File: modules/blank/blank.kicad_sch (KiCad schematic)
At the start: 8 parts

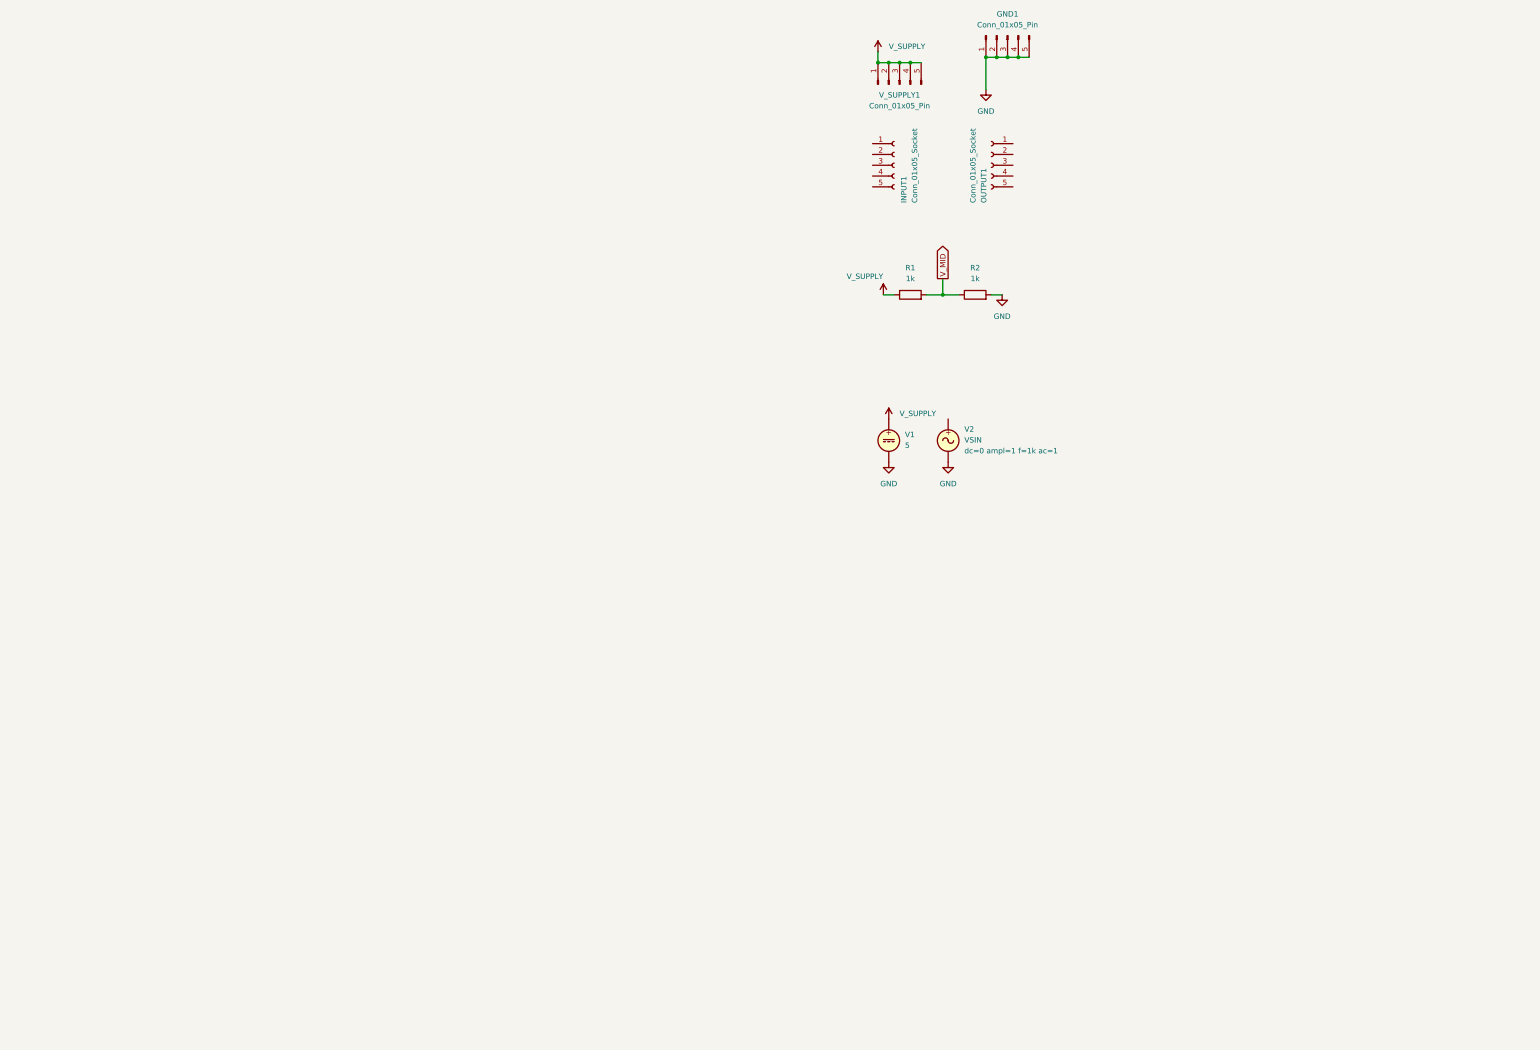
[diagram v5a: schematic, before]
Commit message: blank:Add opamp & pot as a built-in components These are used in almost all the projects. So, having pre-build components make is easy to get started
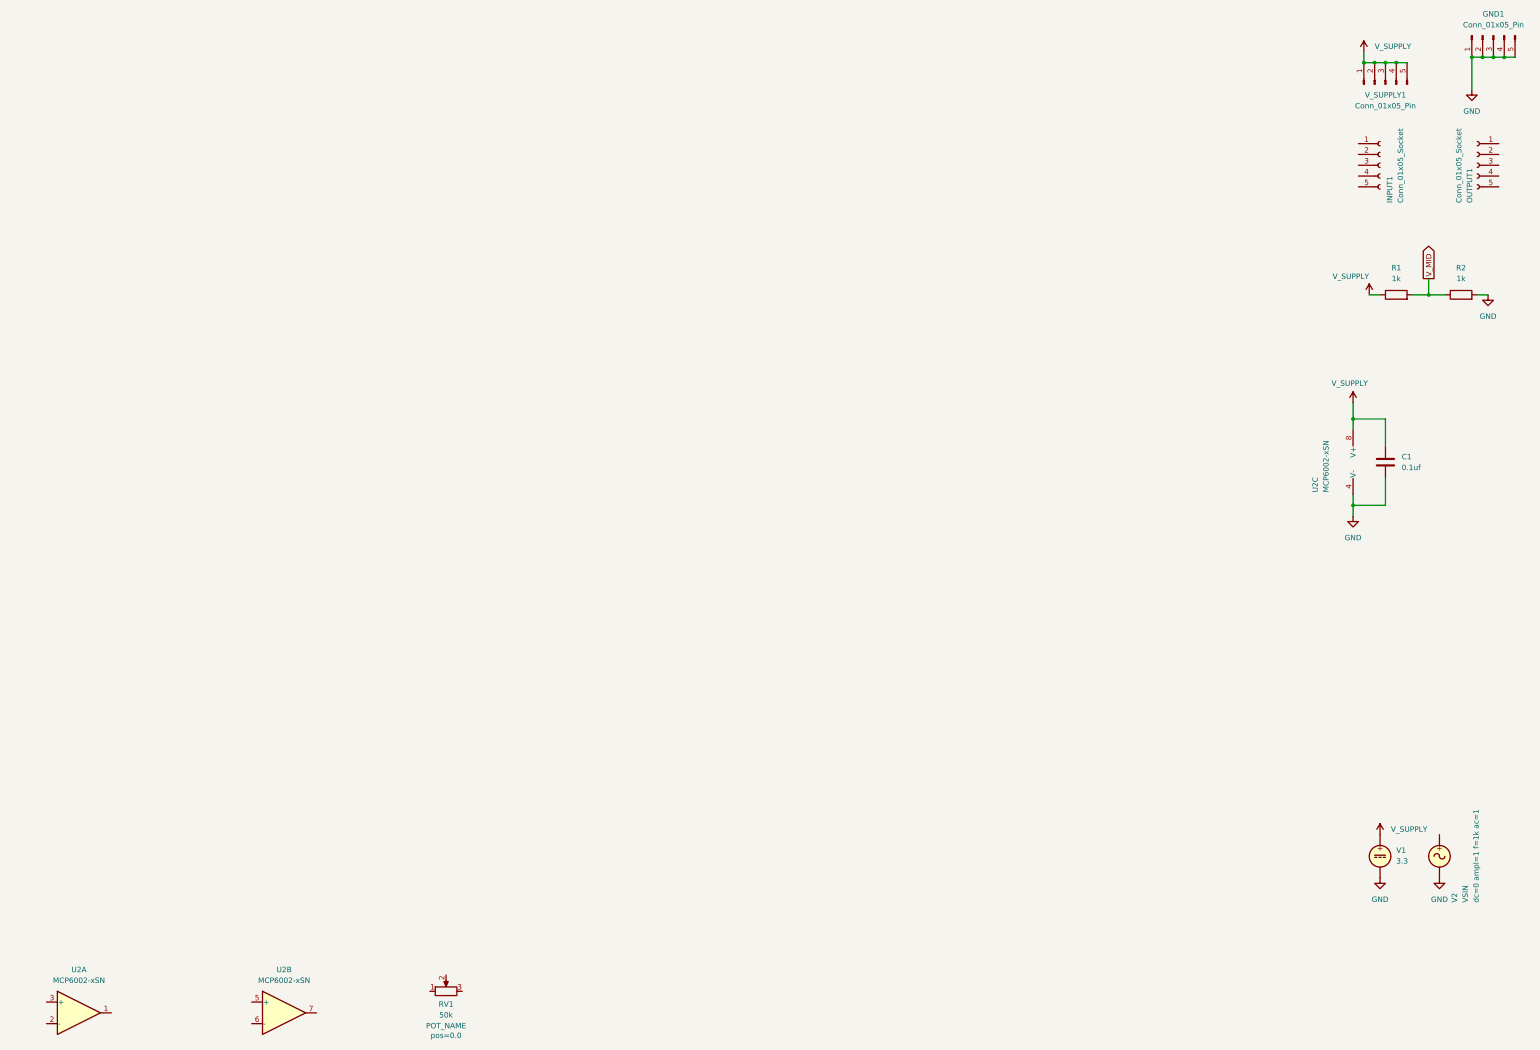
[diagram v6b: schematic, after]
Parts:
- added C1: 0.1uf, symbol Device:C
- added RV1: 50k, BreadModular_Pots:Potentiometer_RV09, symbol Device:R_Potentiometer
- added U2: MCP6002-xSN, Package_SO:SOIC-8-1EP_3.9x4.9mm_P1.27mm_EP2.29x3mm, symbol Amplifier_Operational:MCP6002-xSN
- V1: value 5 -> 3.3
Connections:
- net GND: now also C1.2, U2.4 (V-)
- net V_SUPPLY: now also C1.1, U2.8 (V+)
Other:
- moved on the sheet: GND1, INPUT1, OUTPUT1, R1, R2, V1, V2, V_SUPPLY1
